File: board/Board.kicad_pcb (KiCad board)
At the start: 2 copper layers, 58.5 x 58.5 mm, 72 parts, among them J1 GS3, J10 CONN_01X03, J11 CONN_01X03, J12 GS3, J13 GS3, J14 CONN_01X02, J15 CONN_01X03, J16 GS2, J17 CONN_01X01, J2 CONN_02X04, J3 CONN_01X03, J4 CONN_01X03, J5 CONN_01X03, J6 CONN_01X03, J7 CONN_01X03, J8 CONN_01X03, J9 CONN_01X03, SW1 SW_Push, U1 STM32F410RBTx, U2 SN74LVC1G04, U3 LF33ABDT-TR, U4 ICM-20689, U5 MAG3110, U6 MS5637, Y1 25 MHz

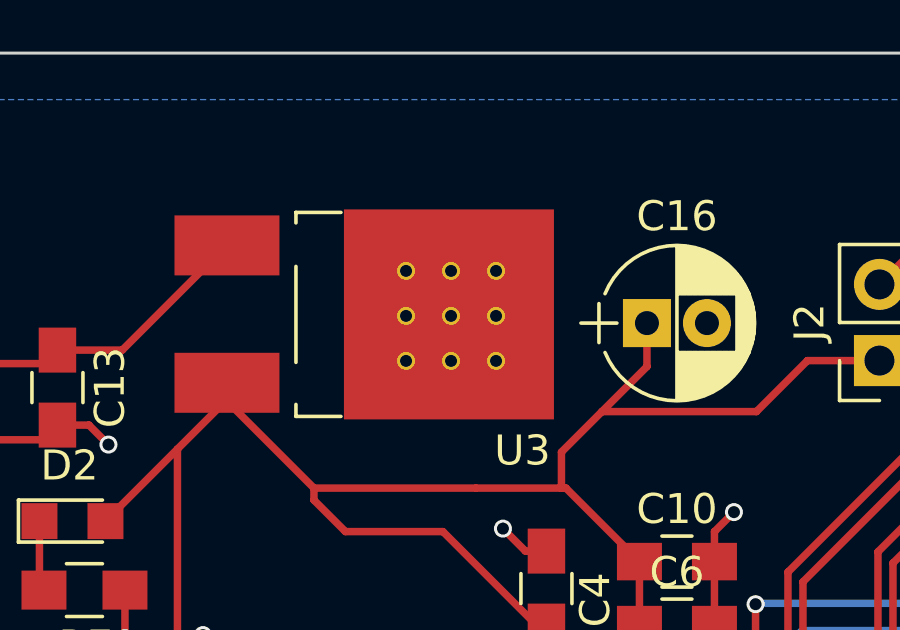
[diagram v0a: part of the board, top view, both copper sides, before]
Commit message: added via stiching
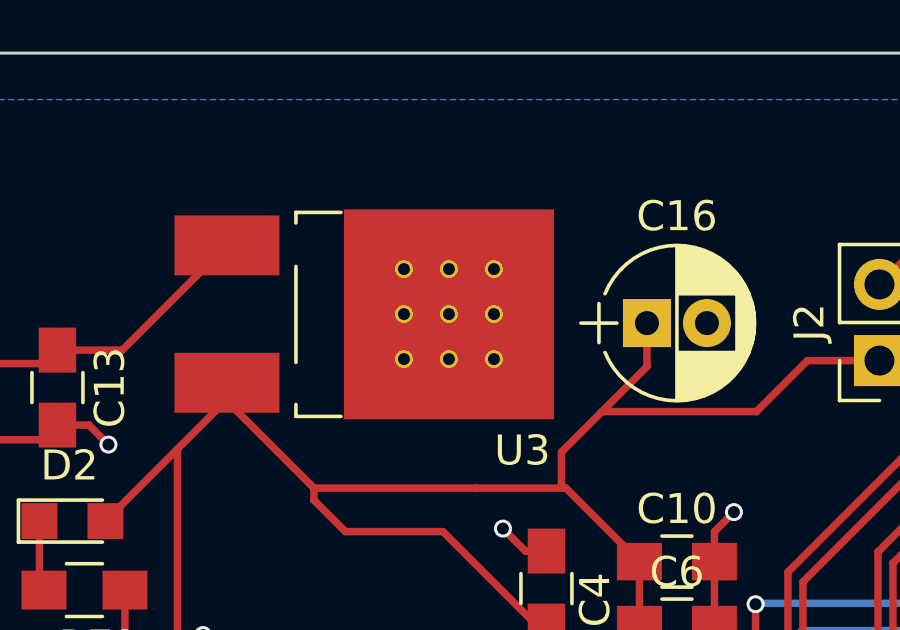
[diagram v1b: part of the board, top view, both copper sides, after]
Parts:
- removed the REF** at (117.8, 74.5)
- removed the REF** at (117.8, 73.0)
- removed the REF** at (119.3, 76.0)
- removed the REF** at (117.8, 76.0)
- removed the REF** at (116.3, 76.0)
- removed the REF** at (119.3, 74.5)
- removed the REF** at (116.3, 74.5)
- removed the REF** at (119.3, 73.0)
- removed the REF** at (116.3, 73.0)
- added REF**: via-0.6mm, via-0.6mm, F.Cu at (119.2, 76.0)
- added REF**: via-0.6mm, via-0.6mm, F.Cu at (117.8, 76.0)
- added REF**: via-0.6mm, via-0.6mm, F.Cu at (116.2, 76.0)
- added REF**: via-0.6mm, via-0.6mm, F.Cu at (119.2, 74.5)
- added REF**: via-0.6mm, via-0.6mm, F.Cu at (117.8, 74.5)
- added REF**: via-0.6mm, via-0.6mm, F.Cu at (116.2, 74.5)
- added REF**: via-0.6mm, via-0.6mm, F.Cu at (119.2, 73.0)
- added REF**: via-0.6mm, via-0.6mm, F.Cu at (117.8, 73.0)
- added REF**: via-0.6mm, via-0.6mm, F.Cu at (116.2, 73.0)
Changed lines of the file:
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@@
 (kicad_pcb (version 4) (host pcbnew 4.0.6)
   (general
-    (links 151)
-    (no_connects 6)
+    (links 160)
+    (no_connects 5)
     (area 95.681217 65.689424 154.310576 124.300001)
     (thickness 1.6)
@@
     (mod_text_size 1 1)
     (mod_text_width 0.15)
-    (pad_size 1.7 1.7)
-    (pad_drill 1)
+    (pad_size 0.6 0.6)
+    (pad_drill 0.4)
     (pad_to_mask_clearance 0)
     (aux_axis_origin 0 0)
@@
   )
   (module via-0.6mm (layer F.Cu)
-    (at 117.82 74.51)
+    (at 119.25 75.95)
     (fp_text reference REF** (at 0 0) (layer F.SilkS) hide
       (effects (font (size 0.127 0.127) (thickness 0.03175)))
@@
       (effects (font (size 0.127 0.127) (thickness 0.03175)))
     )
-    (pad 1 thru_hole circle (at 0 0) (size 0.6 0.6) (drill 0.4) (layers *.Cu))
+    (pad 1 thru_hole circle (at 0 0) (size 0.6 0.6) (drill 0.4) (layers *.Cu)
+      (net 1 GND) (zone_connect 2))
   )
   (module via-0.6mm (layer F.Cu)
-    (at 117.82 73.01)
+    (at 117.75 75.95)
     (fp_text reference REF** (at 0 0) (layer F.SilkS) hide
       (effects (font (size 0.127 0.127) (thickness 0.03175)))
@@
       (effects (font (size 0.127 0.127) (thickness 0.03175)))
     )
-    (pad 1 thru_hole circle (at 0 0) (size 0.6 0.6) (drill 0.4) (layers *.Cu))
+    (pad 1 thru_hole circle (at 0 0) (size 0.6 0.6) (drill 0.4) (layers *.Cu)
+      (net 1 GND) (zone_connect 2))
   )
   (module via-0.6mm (layer F.Cu)
-    (at 119.32 76.01)
+    (at 116.25 75.95)
     (fp_text reference REF** (at 0 0) (layer F.SilkS) hide
       (effects (font (size 0.127 0.127) (thickness 0.03175)))
@@
       (effects (font (size 0.127 0.127) (thickness 0.03175)))
     )
-    (pad 1 thru_hole circle (at 0 0) (size 0.6 0.6) (drill 0.4) (layers *.Cu))
+    (pad 1 thru_hole circle (at 0 0) (size 0.6 0.6) (drill 0.4) (layers *.Cu)
+      (net 1 GND) (zone_connect 2))
   )
   (module via-0.6mm (layer F.Cu)
-    (at 117.82 76.01)
+    (at 119.25 74.45)
     (fp_text reference REF** (at 0 0) (layer F.SilkS) hide
       (effects (font (size 0.127 0.127) (thickness 0.03175)))
@@
       (effects (font (size 0.127 0.127) (thickness 0.03175)))
     )
-    (pad 1 thru_hole circle (at 0 0) (size 0.6 0.6) (drill 0.4) (layers *.Cu))
+    (pad 1 thru_hole circle (at 0 0) (size 0.6 0.6) (drill 0.4) (layers *.Cu)
+      (net 1 GND) (zone_connect 2))
   )
   (module via-0.6mm (layer F.Cu)
-    (at 116.32 76.01)
+    (at 117.75 74.45)
     (fp_text reference REF** (at 0 0) (layer F.SilkS) hide
       (effects (font (size 0.127 0.127) (thickness 0.03175)))
@@
       (effects (font (size 0.127 0.127) (thickness 0.03175)))
     )
-    (pad 1 thru_hole circle (at 0 0) (size 0.6 0.6) (drill 0.4) (layers *.Cu))
+    (pad 1 thru_hole circle (at 0 0) (size 0.6 0.6) (drill 0.4) (layers *.Cu)
+      (net 1 GND) (zone_connect 2))
   )
   (module via-0.6mm (layer F.Cu)
-    (at 119.32 74.51)
+    (at 116.25 74.45)
     (fp_text reference REF** (at 0 0) (layer F.SilkS) hide
       (effects (font (size 0.127 0.127) (thickness 0.03175)))
@@
       (effects (font (size 0.127 0.127) (thickness 0.03175)))
     )
-    (pad 1 thru_hole circle (at 0 0) (size 0.6 0.6) (drill 0.4) (layers *.Cu))
+    (pad 1 thru_hole circle (at 0 0) (size 0.6 0.6) (drill 0.4) (layers *.Cu)
+      (net 1 GND) (zone_connect 2))
   )
   (module via-0.6mm (layer F.Cu)
-    (at 116.32 74.51)
+    (at 119.25 72.95)
     (fp_text reference REF** (at 0 0) (layer F.SilkS) hide
       (effects (font (size 0.127 0.127) (thickness 0.03175)))
@@
       (effects (font (size 0.127 0.127) (thickness 0.03175)))
     )
-    (pad 1 thru_hole circle (at 0 0) (size 0.6 0.6) (drill 0.4) (layers *.Cu))
+    (pad 1 thru_hole circle (at 0 0) (size 0.6 0.6) (drill 0.4) (layers *.Cu)
+      (net 1 GND) (zone_connect 2))
   )
   (module via-0.6mm (layer F.Cu)
-    (at 119.32 73.01)
+    (at 117.75 72.95)
     (fp_text reference REF** (at 0 0) (layer F.SilkS) hide
       (effects (font (size 0.127 0.127) (thickness 0.03175)))
@@
       (effects (font (size 0.127 0.127) (thickness 0.03175)))
     )
-    (pad 1 thru_hole circle (at 0 0) (size 0.6 0.6) (drill 0.4) (layers *.Cu))
+    (pad 1 thru_hole circle (at 0 0) (size 0.6 0.6) (drill 0.4) (layers *.Cu)
+      (net 1 GND) (zone_connect 2))
   )
   (module via-0.6mm (layer F.Cu)
-    (at 116.32 73.01)
+    (at 116.25 72.95)
     (fp_text reference REF** (at 0 0) (layer F.SilkS) hide
       (effects (font (size 0.127 0.127) (thickness 0.03175)))
@@
       (effects (font (size 0.127 0.127) (thickness 0.03175)))
     )
-    (pad 1 thru_hole circle (at 0 0) (size 0.6 0.6) (drill 0.4) (layers *.Cu))
+    (pad 1 thru_hole circle (at 0 0) (size 0.6 0.6) (drill 0.4) (layers *.Cu)
+      (net 1 GND) (zone_connect 2))
   )
   (module Local_prints:DFN_2x2mm_10pin_0.4pitch (layer F.Cu)
@@
     (min_thickness 0.254)
     (keepout (tracks not_allowed) (vias not_allowed) (copperpour not_allowed))
-    (fill (arc_segments 16) (thermal_gap 0.508) (thermal_bridge_width 0.508))
+    (fill yes (arc_segments 16) (thermal_gap 0.508) (thermal_bridge_width 0.508))
     (polygon
       (pts

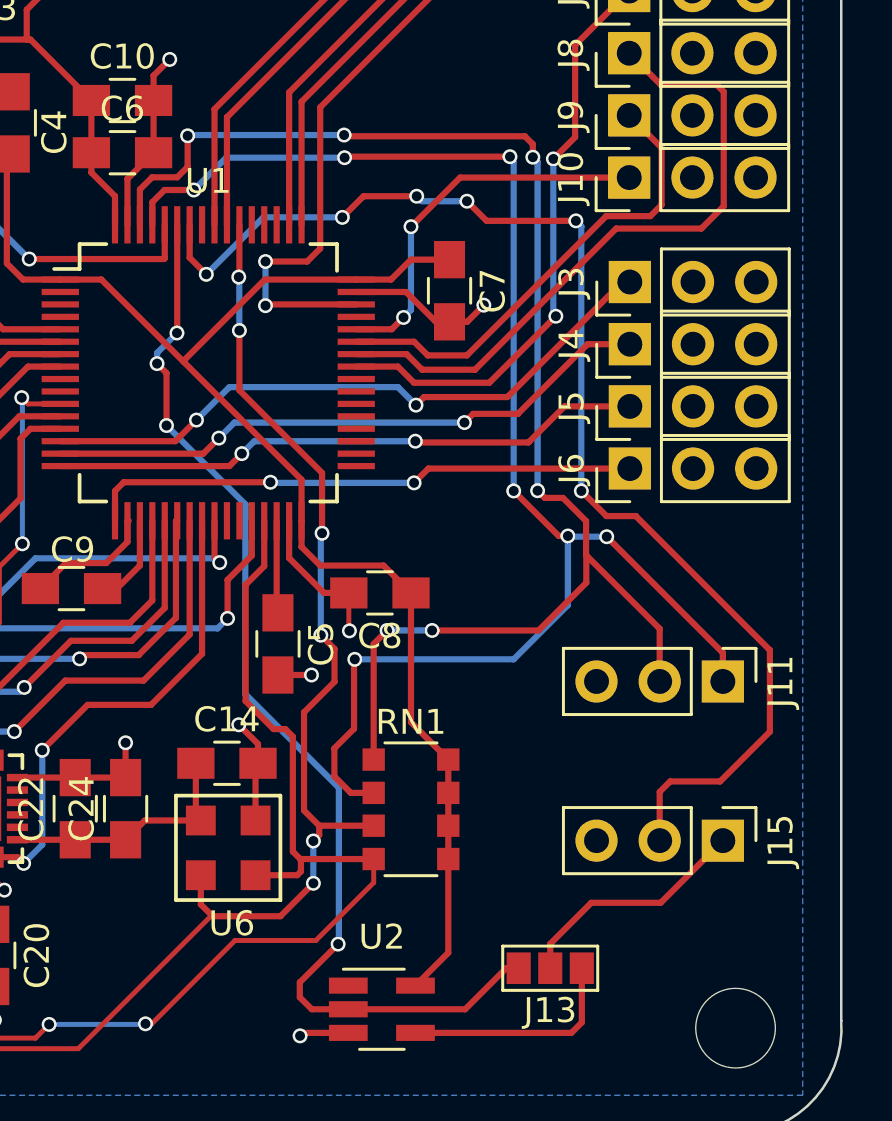
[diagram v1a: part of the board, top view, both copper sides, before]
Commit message: exposed another UART
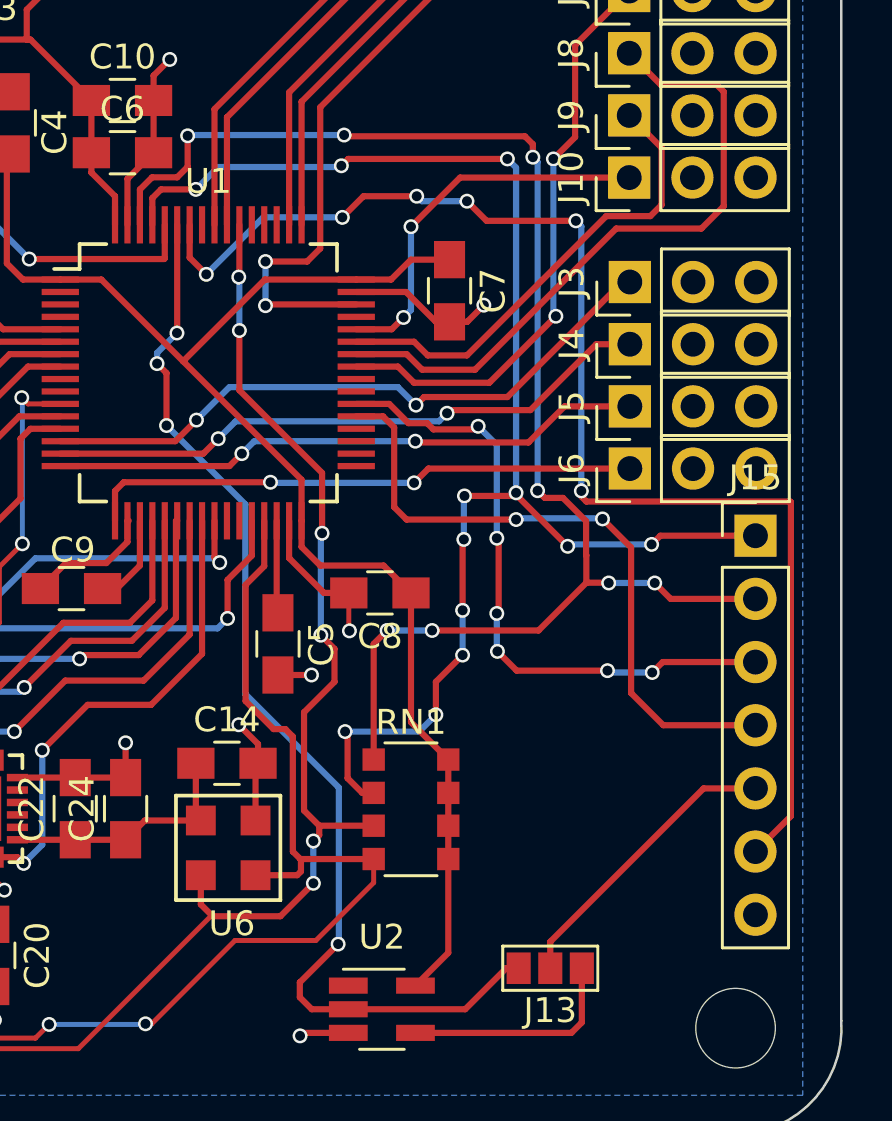
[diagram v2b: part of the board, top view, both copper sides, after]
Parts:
- removed J11: CONN_01X03, Pin_Headers:Pin_Header_Straight_1x03_Pitch2.54mm
- J15: value CONN_01X03 -> CONN_01X07; footprint Pin_Headers:Pin_Header_Straight_1x03_Pitch2.54mm -> Pin_Headers:Pin_Header_Straight_1x07_Pitch2.54mm
- moved J15 12.3 mm to (150.8, 100.2), turned to 0 degrees
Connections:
- net UART_RX renamed UART1_RX
- J15 pad 1: Net-(J13-Pad2) -> I2C1_SCL
- J15 pad 2: UART_TX -> I2C1_SDA
- J15 pad 3: GND -> UART2_RX
- U1 pad 37: Net-(U1-Pad37) -> UART2_TX
- U1 pad 38: Net-(U1-Pad38) -> UART2_RX
- U1 pad 58: UART_TX -> UART1_TX
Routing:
- net UART1_TX: track 0.00 -> 53.2 mm, vias 0 -> 6
- net UART_TX: track 50.7 -> 0.00 mm, vias 6 -> 0
- net UART2_TX: track 0.00 -> 26.5 mm, vias 0 -> 2
- net UART2_RX: track 0.00 -> 25.7 mm, vias 0 -> 6
- net Net-(J13-Pad2): track 9.64 -> 11.9 mm
- net I2C1_SCL: track 61.0 -> 58.9 mm, vias 7 -> 12
- net I2C1_SDA: track 58.5 -> 59.2 mm, vias 6 -> 8

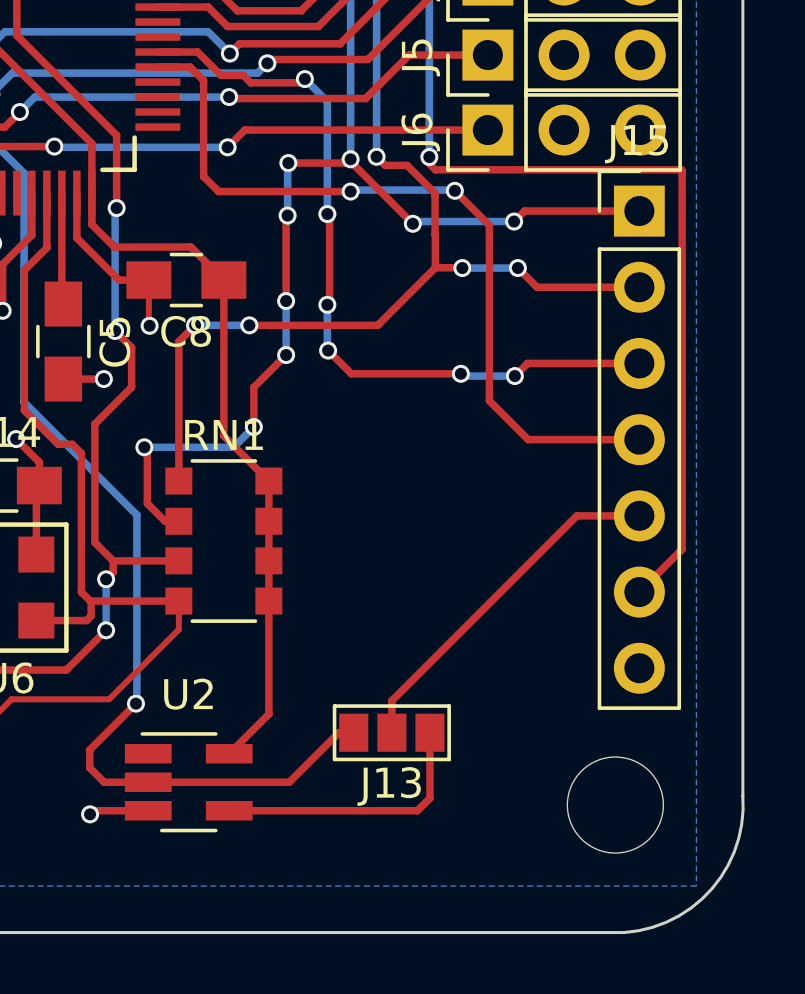
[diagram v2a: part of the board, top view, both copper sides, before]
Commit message: silk screen items
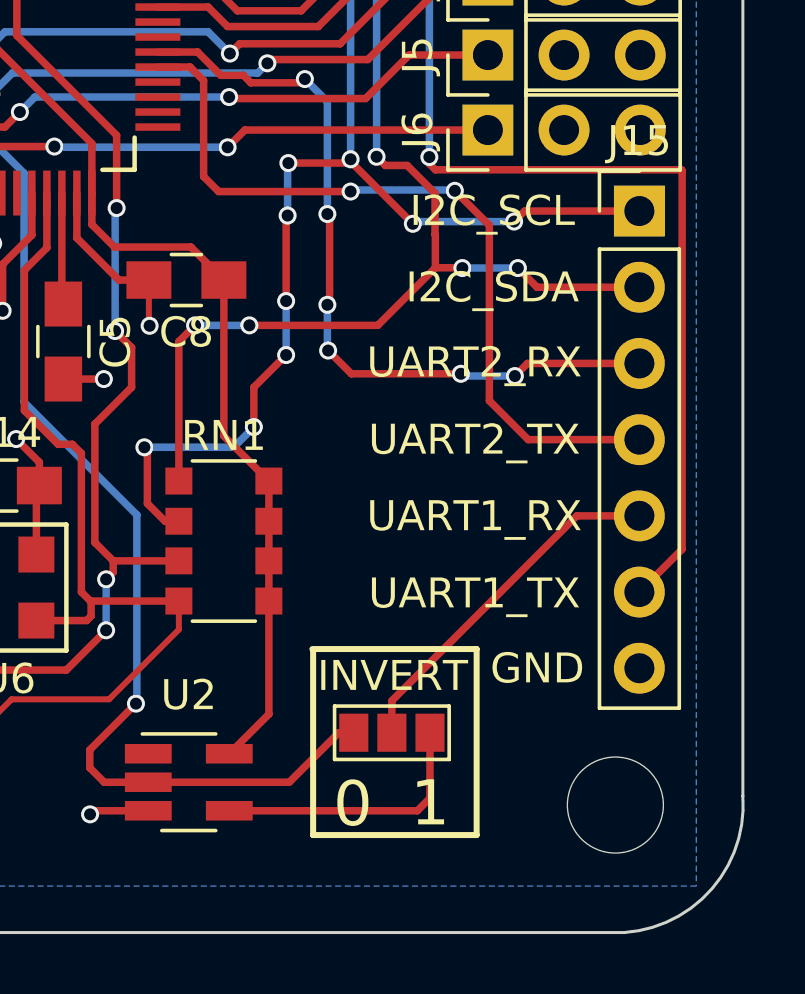
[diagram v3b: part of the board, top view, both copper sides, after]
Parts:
- renumbered J13 to ?
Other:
- board text added: "0"
- board text added: "1"
- board text added: "GND"
- board text added: "I2C_SCL"
- board text added: "I2C_SDA"
- board text added: "INVERT"
- board text added: "UART1_RX"
- board text added: "UART1_TX"
- board text added: "UART2_RX"
- board text added: "UART2_TX"
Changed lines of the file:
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@@
     (area 95.681217 65.689424 154.310576 124.300001)
     (thickness 1.6)
-    (drawings 8)
+    (drawings 22)
     (tracks 766)
     (zones 0)
@@
   (page A4)
   (layers
-    (0 F.Cu signal)
-    (31 B.Cu signal)
+    (0 F.Cu signal hide)
+    (31 B.Cu signal hide)
     (32 B.Adhes user)
     (33 F.Adhes user)
@@
     (tags "solder bridge")
     (attr smd)
-    (fp_text reference J13 (at -1.7 0 180) (layer F.SilkS)
+    (fp_text reference "" (at -1.7 0 180) (layer F.SilkS)
       (effects (font (size 1 1) (thickness 0.15)))
     )
@@
     )
   )
+  (gr_line (start 145.375 114.8) (end 139.9 114.8) (angle 90) (layer F.SilkS) (width 0.2))
+  (gr_line (start 145.375 121) (end 145.375 114.8) (angle 90) (layer F.SilkS) (width 0.2))
+  (gr_line (start 139.925 121) (end 145.375 121) (angle 90) (layer F.SilkS) (width 0.2))
+  (gr_line (start 139.925 114.85) (end 139.925 121) (angle 90) (layer F.SilkS) (width 0.2))
+  (gr_text 0 (at 141.25 119.975) (layer F.SilkS)
+    (effects (font (size 1.5 1.5) (thickness 0.3)))
+  )
+  (gr_text 1 (at 143.825 119.95) (layer F.SilkS)
+    (effects (font (size 1.5 1.5) (thickness 0.3)))
+  )
+  (gr_text INVERT (at 142.575 115.7) (layer F.SilkS)
+    (effects (font (size 1 1) (thickness 0.2)))
+  )
+  (gr_text GND (at 147.4 115.45) (layer F.SilkS)
+    (effects (font (size 1 1) (thickness 0.2)))
+  )
+  (gr_text UART1_TX (at 145.3 112.95) (layer F.SilkS)
+    (effects (font (size 1 1) (thickness 0.2)))
+  )
+  (gr_text UART1_RX (at 145.3 110.375) (layer F.SilkS)
+    (effects (font (size 1 1) (thickness 0.2)))
+  )
+  (gr_text UART2_TX (at 145.3 107.825) (layer F.SilkS)
+    (effects (font (size 1 1) (thickness 0.2)))
+  )
+  (gr_text UART2_RX (at 145.3 105.25) (layer F.SilkS)
+    (effects (font (size 1 1) (thickness 0.2)))
+  )
+  (gr_text I2C_SDA (at 145.9 102.75) (layer F.SilkS)
+    (effects (font (size 1 1) (thickness 0.2)))
+  )
+  (gr_text I2C_SCL (at 145.9 100.2) (layer F.SilkS)
+    (effects (font (size 1 1) (thickness 0.2)))
+  )
   (gr_line (start 100.3 65.75) (end 150.2 65.75) (angle 90) (layer Edge.Cuts) (width 0.1))
